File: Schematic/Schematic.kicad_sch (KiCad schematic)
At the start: 0 parts

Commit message: Added stuff from today
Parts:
- added H1, H2, H3, H4: MountingHole, MountingHole:MountingHole_5mm, symbol Mechanical:MountingHole
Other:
- added sheet Extra Points (extra_points.kicad_sch)
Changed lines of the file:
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@@
 (kicad_sch (version 20230121) (generator eeschema)
   (paper "A4")
+  (symbol (lib_id "Mechanical:MountingHole") (at 248.92 26.67 0) (unit 1)
+    (in_bom yes) (on_board yes) (dnp no) (fields_autoplaced)
+    (property "Reference" "H2" (at 251.46 26.035 0)
+      (effects (font (size 1.27 1.27)) (justify left))
+    )
+    (property "Value" "MountingHole" (at 251.46 28.575 0)
+      (effects (font (size 1.27 1.27)) (justify left))
+    )
+    (property "Footprint" "MountingHole:MountingHole_5mm" (at 248.92 26.67 0)
+      (effects (font (size 1.27 1.27)) hide)
+    )
+    (property "Datasheet" "~" (at 248.92 26.67 0)
+      (effects (font (size 1.27 1.27)) hide)
+    )
+    (instances
+      (project "Schematic"
+        (path "/ced54cd9-3b34-40e4-aa66-964aaab81b0a/49528601-a054-44d2-8cd6-b055d7d9a1ef"
+          (reference "H2") (unit 1)
+        )
+        (path "/ced54cd9-3b34-40e4-aa66-964aaab81b0a"
+          (reference "H2") (unit 1)
+        )
+      )
+    )
+  )
+  (symbol (lib_id "Mechanical:MountingHole") (at 248.92 36.83 0) (unit 1)
+    (in_bom yes) (on_board yes) (dnp no) (fields_autoplaced)
+    (property "Reference" "H4" (at 251.46 36.195 0)
+      (effects (font (size 1.27 1.27)) (justify left))
+    )
+    (property "Value" "MountingHole" (at 251.46 38.735 0)
+      (effects (font (size 1.27 1.27)) (justify left))
+    )
+    (property "Footprint" "MountingHole:MountingHole_5mm" (at 248.92 36.83 0)
+      (effects (font (size 1.27 1.27)) hide)
+    )
+    (property "Datasheet" "~" (at 248.92 36.83 0)
+      (effects (font (size 1.27 1.27)) hide)
+    )
+    (instances
+      (project "Schematic"
+        (path "/ced54cd9-3b34-40e4-aa66-964aaab81b0a/49528601-a054-44d2-8cd6-b055d7d9a1ef"
+          (reference "H4") (unit 1)
+        )
+        (path "/ced54cd9-3b34-40e4-aa66-964aaab81b0a"
+          (reference "H4") (unit 1)
+        )
+      )
+    )
+  )
+  (symbol (lib_id "Mechanical:MountingHole") (at 248.92 21.59 0) (unit 1)
+    (in_bom yes) (on_board yes) (dnp no) (fields_autoplaced)
+    (property "Reference" "H1" (at 251.46 20.955 0)
+      (effects (font (size 1.27 1.27)) (justify left))
+    )
+    (property "Value" "MountingHole" (at 251.46 23.495 0)
+      (effects (font (size 1.27 1.27)) (justify left))
+    )
+    (property "Footprint" "MountingHole:MountingHole_5mm" (at 248.92 21.59 0)
+      (effects (font (size 1.27 1.27)) hide)
+    )
+    (property "Datasheet" "~" (at 248.92 21.59 0)
+      (effects (font (size 1.27 1.27)) hide)
+    )
+    (instances
+      (project "Schematic"
+        (path "/ced54cd9-3b34-40e4-aa66-964aaab81b0a/49528601-a054-44d2-8cd6-b055d7d9a1ef"
+          (reference "H1") (unit 1)
+        )
+        (path "/ced54cd9-3b34-40e4-aa66-964aaab81b0a"
+          (reference "H1") (unit 1)
+        )
+      )
+    )
+  )
+  (symbol (lib_id "Mechanical:MountingHole") (at 248.92 31.75 0) (unit 1)
+    (in_bom yes) (on_board yes) (dnp no) (fields_autoplaced)
+    (property "Reference" "H3" (at 251.46 31.115 0)
+      (effects (font (size 1.27 1.27)) (justify left))
+    )
+    (property "Value" "MountingHole" (at 251.46 33.655 0)
+      (effects (font (size 1.27 1.27)) (justify left))
+    )
+    (property "Footprint" "MountingHole:MountingHole_5mm" (at 248.92 31.75 0)
+      (effects (font (size 1.27 1.27)) hide)
+    )
+    (property "Datasheet" "~" (at 248.92 31.75 0)
+      (effects (font (size 1.27 1.27)) hide)
+    )
+    (instances
+      (project "Schematic"
+        (path "/ced54cd9-3b34-40e4-aa66-964aaab81b0a/49528601-a054-44d2-8cd6-b055d7d9a1ef"
+          (reference "H3") (unit 1)
+        )
+        (path "/ced54cd9-3b34-40e4-aa66-964aaab81b0a"
+          (reference "H3") (unit 1)
+        )
+      )
+    )
+  )
   (sheet (at 73.66 114.3) (size 66.04 29.21) (fields_autoplaced)
     (stroke (width 0.1524) (type solid))
@@
       )
     )
+  )
+  (sheet (at 154.94 123.19) (size 12.7 3.81) (fields_autoplaced)
+    (stroke (width 0.1524) (type solid))
+    (fill (color 0 0 0 0.0000))
+    (property "Sheetname" "Extra Points" (at 154.94 122.4784 0)
+      (effects (font (size 1.27 1.27)) (justify left bottom))
+    )
+    (property "Sheetfile" "extra_points.kicad_sch" (at 154.94 127.5846 0)
+      (effects (font (size 1.27 1.27)) (justify left top))
+    )
+    (instances
+      (project "Schematic"
+        (path "/ced54cd9-3b34-40e4-aa66-964aaab81b0a" (page "8"))
+      )
+    )

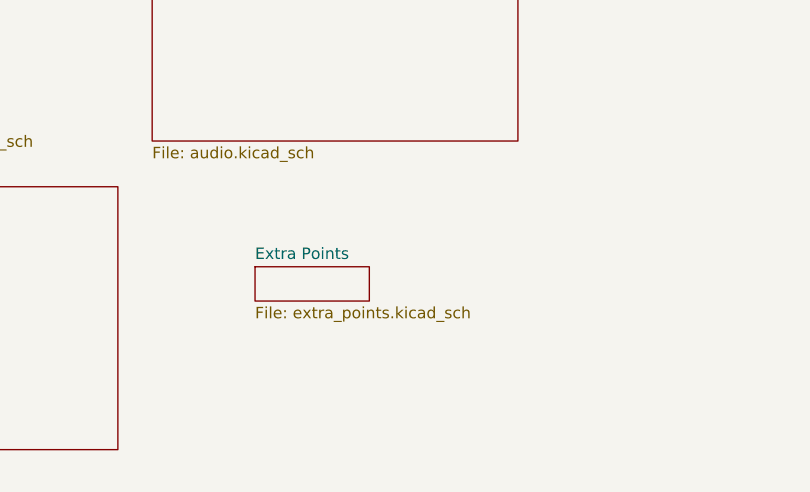
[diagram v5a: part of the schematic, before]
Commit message: Added sensors. Fixed other stuff.
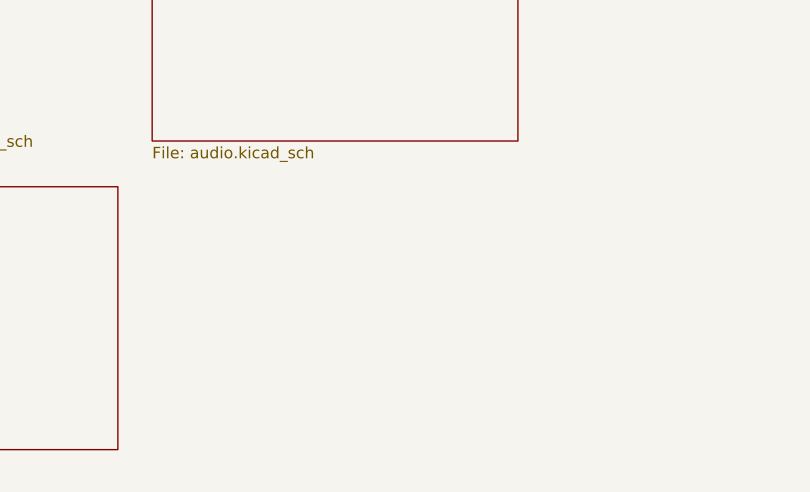
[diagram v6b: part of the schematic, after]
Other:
- removed sheet Extra Points
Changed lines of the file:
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@@
-    )
-  )
-  (sheet (at 154.94 123.19) (size 12.7 3.81) (fields_autoplaced)
-    (stroke (width 0.1524) (type solid))
-    (fill (color 0 0 0 0.0000))
-    (property "Sheetname" "Extra Points" (at 154.94 122.4784 0)
-      (effects (font (size 1.27 1.27)) (justify left bottom))
-    )
-    (property "Sheetfile" "extra_points.kicad_sch" (at 154.94 127.5846 0)
-      (effects (font (size 1.27 1.27)) (justify left top))
-    )
-    (instances
-      (project "Schematic"
-        (path "/ced54cd9-3b34-40e4-aa66-964aaab81b0a" (page "8"))
-      )
     )
   )

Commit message: Added level shifter (may or may not use) other minor fixes
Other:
- added sheet WS2812B (ws2812b.kicad_sch)
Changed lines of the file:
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@@
+    )
+  )
+  (sheet (at 152.4 115.57) (size 35.56 27.94) (fields_autoplaced)
+    (stroke (width 0.1524) (type solid))
+    (fill (color 0 0 0 0.0000))
+    (property "Sheetname" "WS2812B" (at 152.4 114.8584 0)
+      (effects (font (size 1.27 1.27)) (justify left bottom))
+    )
+    (property "Sheetfile" "ws2812b.kicad_sch" (at 152.4 144.0946 0)
+      (effects (font (size 1.27 1.27)) (justify left top))
+    )
+    (instances
+      (project "Schematic"
+        (path "/ced54cd9-3b34-40e4-aa66-964aaab81b0a" (page "8"))
+      )
     )
   )
